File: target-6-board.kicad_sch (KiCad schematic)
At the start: 42 parts, among them J1 Conn_01x10_Socket, J10 RJ14, J11 RJ14, J12 RJ14, J13 RJ14, J14 RJ14, J15 RJ14, J2 Conn_01x12_Socket, J3 Conn_01x10_Socket, J4 Conn_01x12_Socket, J9 RJ14, Q0 NMOS, Q1 NMOS, Q2 NMOS, Q3 NMOS, Q4 NMOS, Q5 NMOS, Q6 NMOS, Q7 NMOS

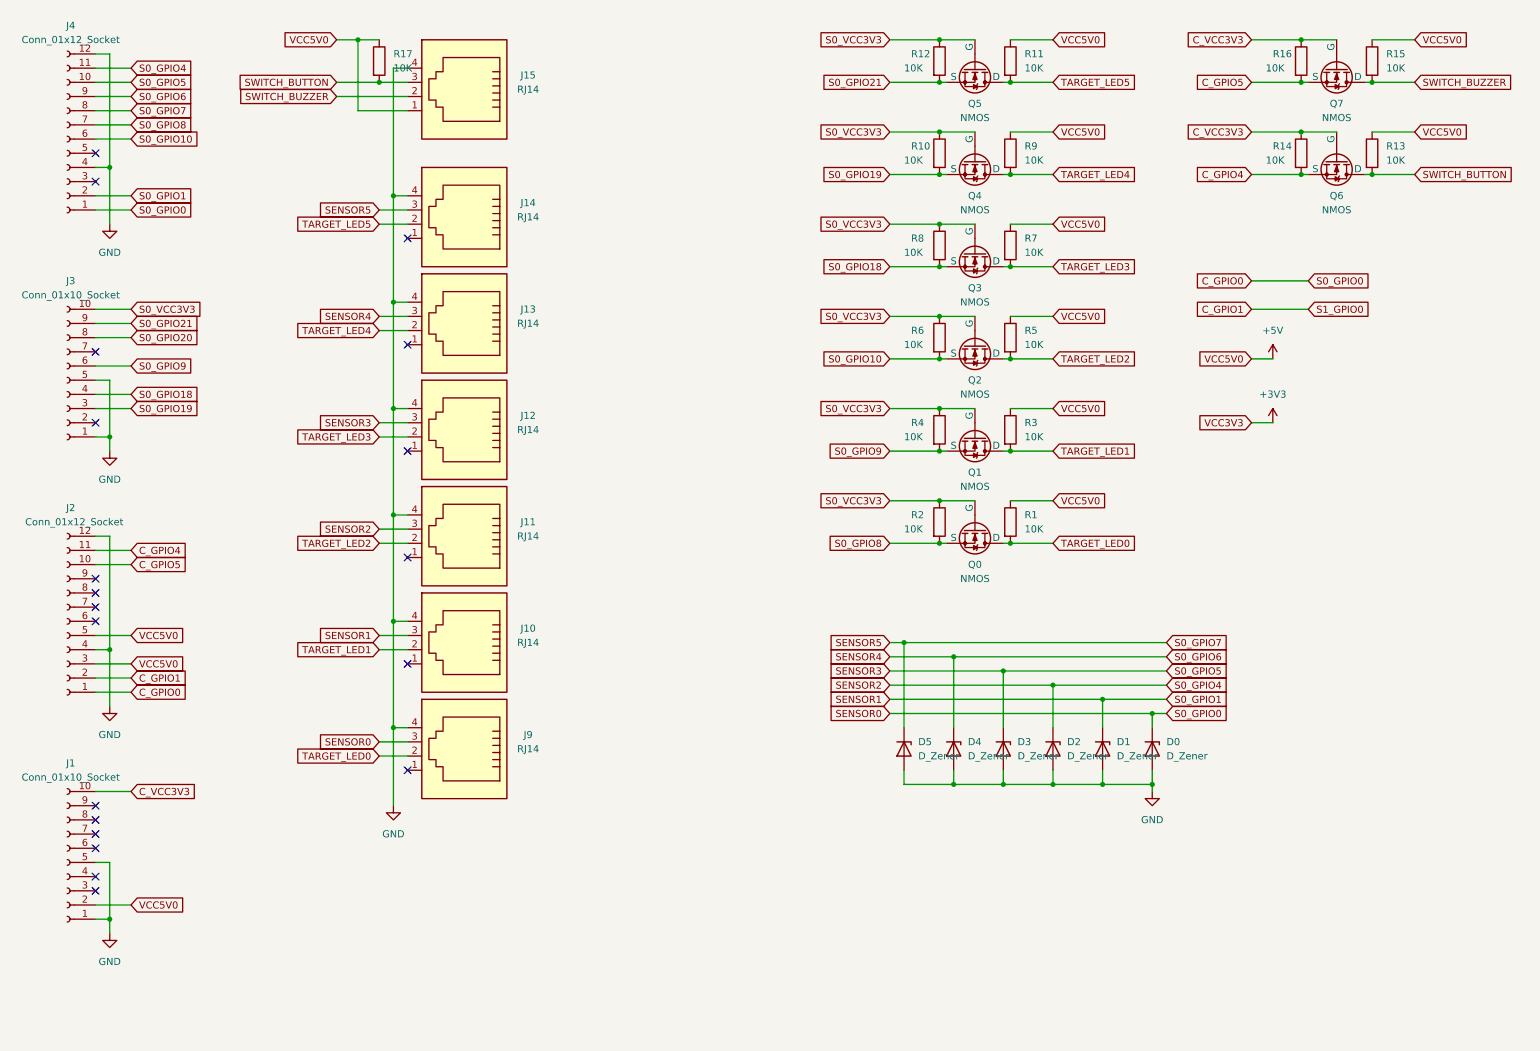
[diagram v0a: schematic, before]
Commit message: PCB order version
- Add USB connectors for power supply to M5Stamp C3
- Add RJ14 connectors for multiplay
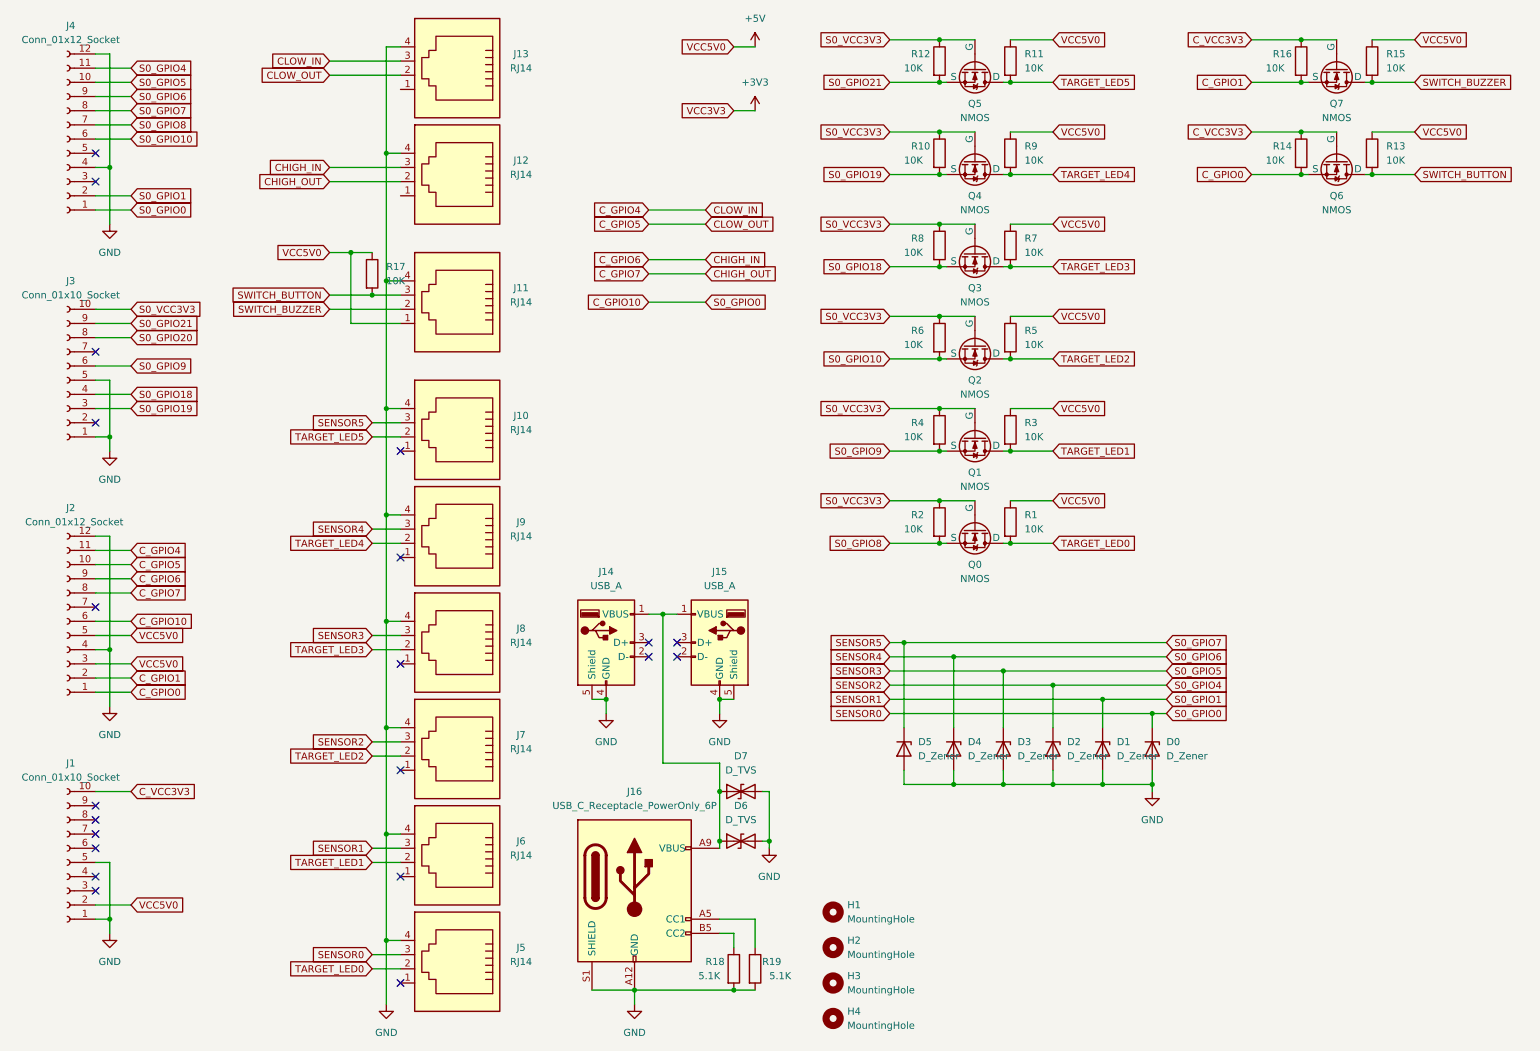
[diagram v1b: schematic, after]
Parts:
- added D6, D7: D_TVS, Diode_SMD:D_SOD-323, symbol Device:D_TVS
- added H1, H2, H3, H4: MountingHole, MountingHole:MountingHole_3.2mm_M3_ISO14580, symbol Mechanical:MountingHole
- added J12, J13: RJ14, Connector_RJ:RJ14_Connfly_DS1133-S4_Horizontal, symbol Connector:RJ14
- added J14, J15: USB_A, Connector_USB:USB_A_Molex_67643_Horizontal, symbol Connector:USB_A
- added J16: USB_C_Receptacle_PowerOnly_6P, Connector_USB:USB_C_Receptacle_GCT_USB4125-xx-x_6P_TopMnt_Horizontal, symbol Connector:USB_C_Receptacle_PowerOnly_6P
- added R18, R19: 5.1K, Resistor_SMD:R_0603_1608Metric, symbol Device:R
- renumbered J14 to J10, J15 to J11, J9 to J5, J10 to J6, J11 to J7, J12 to J8, J13 to J9
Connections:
- net C_GPIO0: now also Q6.3 (S), R14.2; no longer D0.1 (K), J4.1 (Pin_1), J5.3
- net C_GPIO1: now also Q7.3 (S), R16.2
- net GND: now also D6.2 (A2), D7.2 (A2), J12.4, J13.4, J14.4 (GND), J14.5 (Shield), J15.4 (GND), J15.5 (Shield), J16.A12 (GND), J16.B12 (GND), J16.S1 (SHIELD), R18.2, R19.2
- net C_GPIO10: now reaches J2.6 (Pin_6)
- net C_GPIO10: now also D0.1 (K), J4.1 (Pin_1), J5.3
- net CHIGH_OUT: now reaches J2.8 (Pin_8)
- net CHIGH_OUT: now also J12.2
- net CHIGH_IN: now reaches J2.9 (Pin_9)
- net CHIGH_IN: now also J12.3
- removed net C_GPIO4: J2.11 (Pin_11), Q6.3 (S), R14.2
- removed net C_GPIO5: J2.10 (Pin_10), Q7.3 (S), R16.2
- new net: D6.1 (A1), D7.1 (A1), J14.1 (VBUS), J15.1 (VBUS), J16.A9 (VBUS), J16.B9 (VBUS)
- new net: J16.A5 (CC1), R19.1
- new net: J16.B5 (CC2), R18.1
- new net CLOW_IN: J13.3, J2.11 (Pin_11)
- new net CLOW_OUT: J13.2, J2.10 (Pin_10)
- no-connect marks 20 -> 21
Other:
- moved on the sheet: J10, J11, J5, J6, J7, J8, J9, R17
